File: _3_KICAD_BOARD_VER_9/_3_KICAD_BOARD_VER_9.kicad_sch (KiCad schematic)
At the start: 0 parts

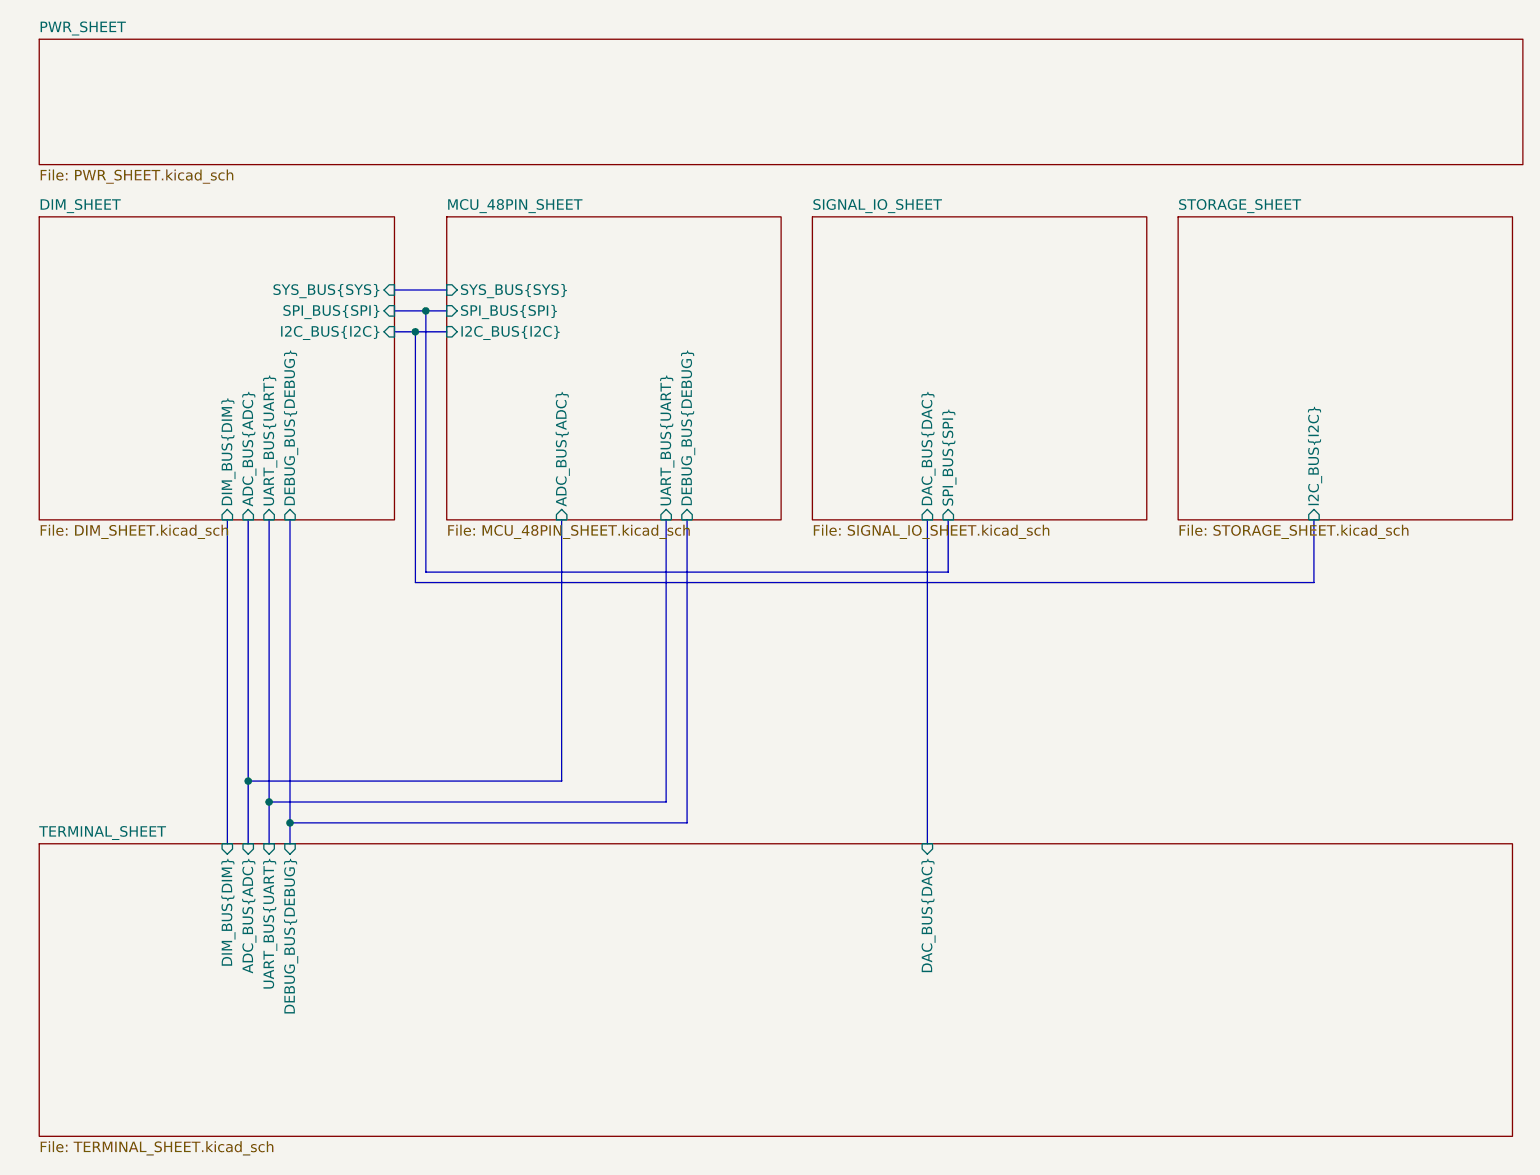
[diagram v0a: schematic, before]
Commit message: feat : vdd, gnd, vin routing done
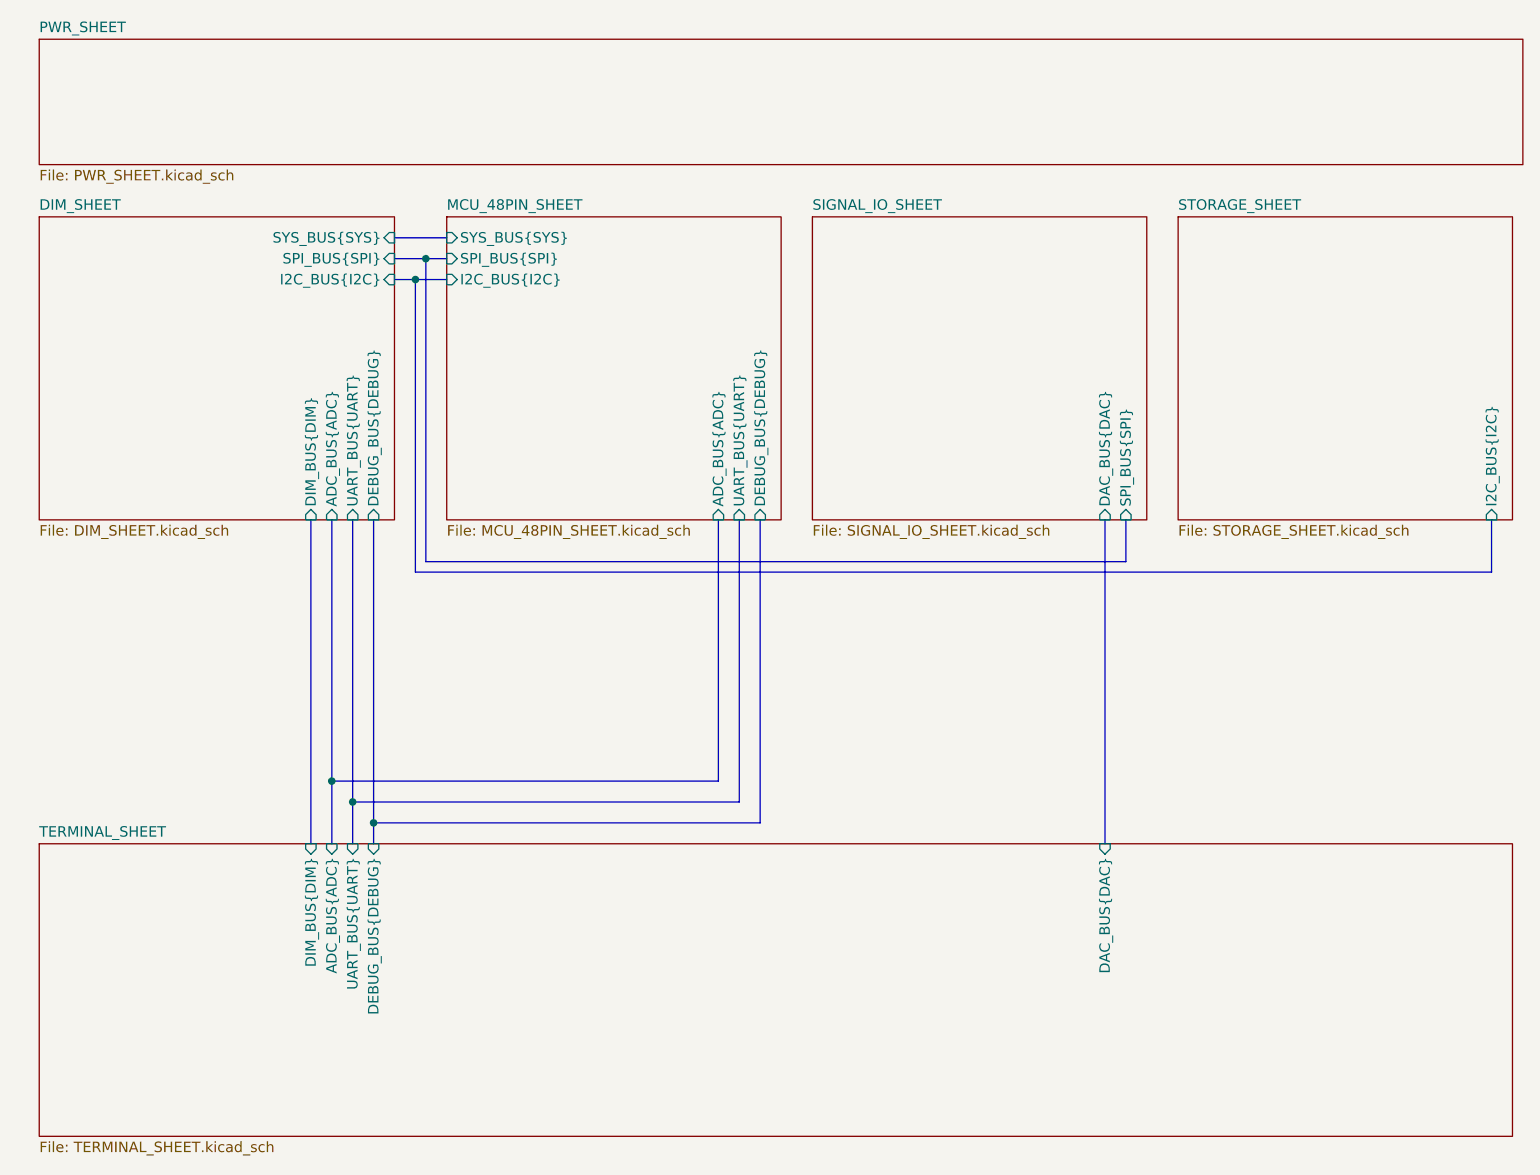
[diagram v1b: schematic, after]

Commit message: feat : dim only project done
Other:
- removed sheet DIM_SHEET
- sheet TERMINAL_SHEET ports: added SYS_BUS{SYS}; removed DIM_BUS{DIM}

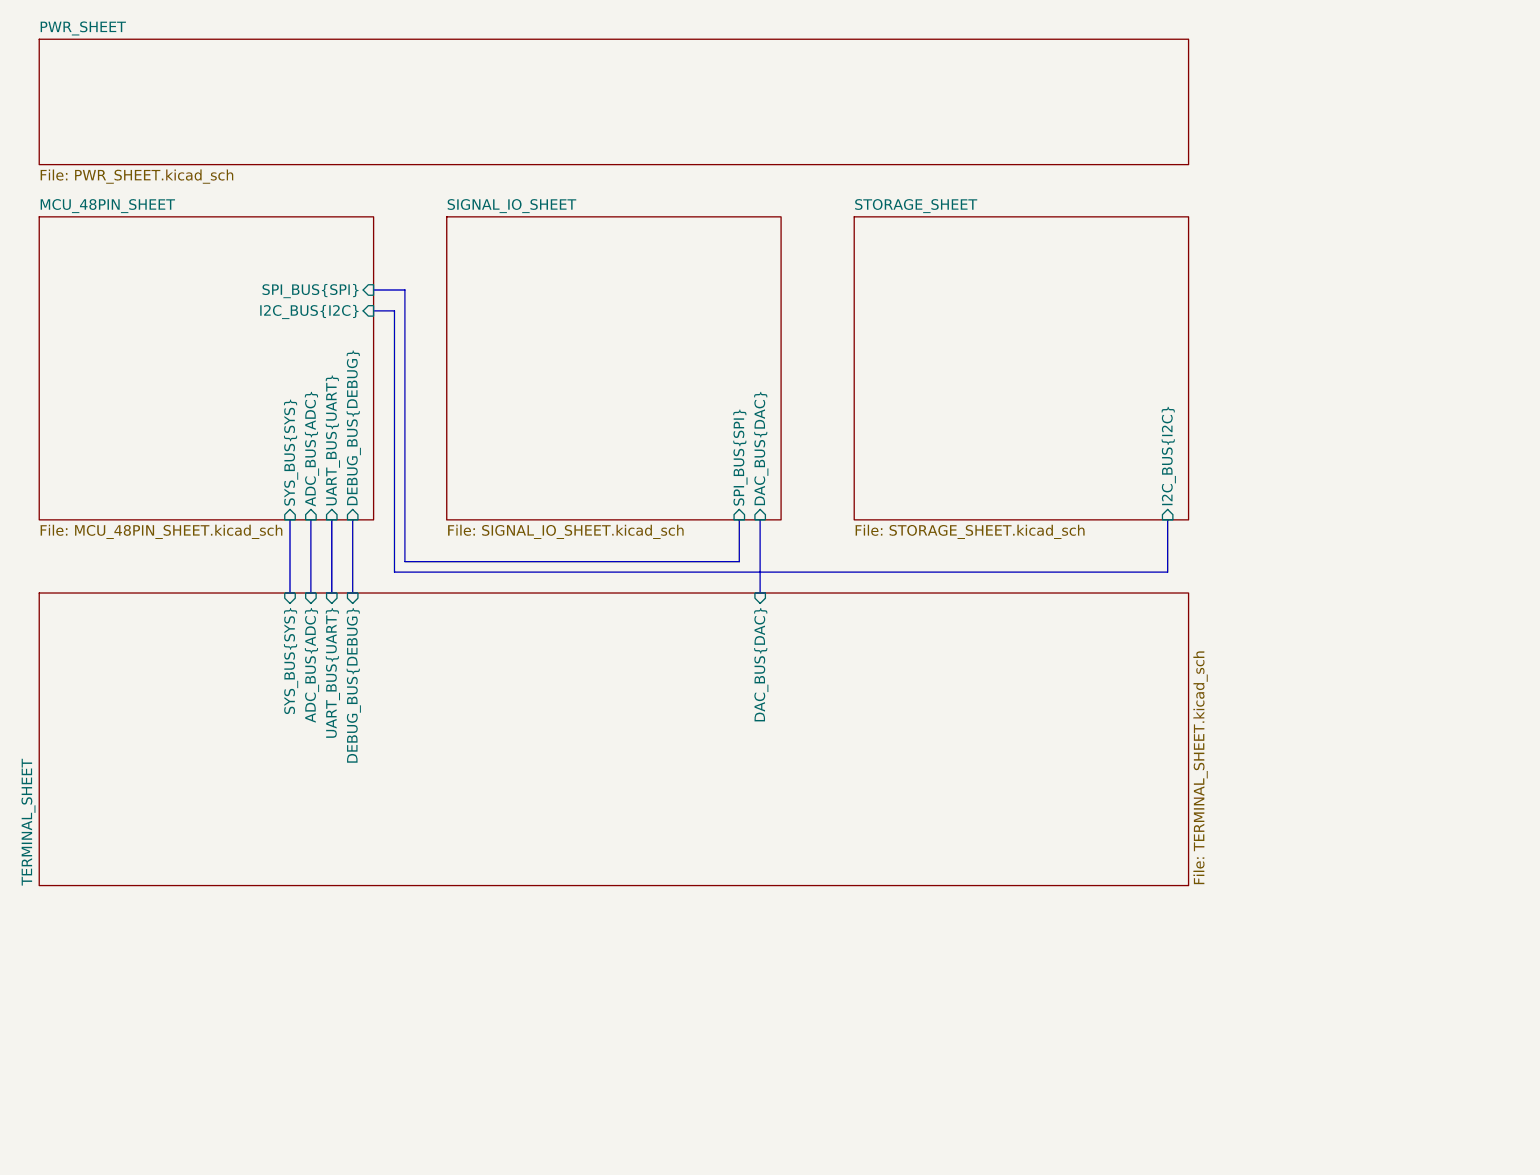
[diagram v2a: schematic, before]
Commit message: feat : 회로도 업데이트
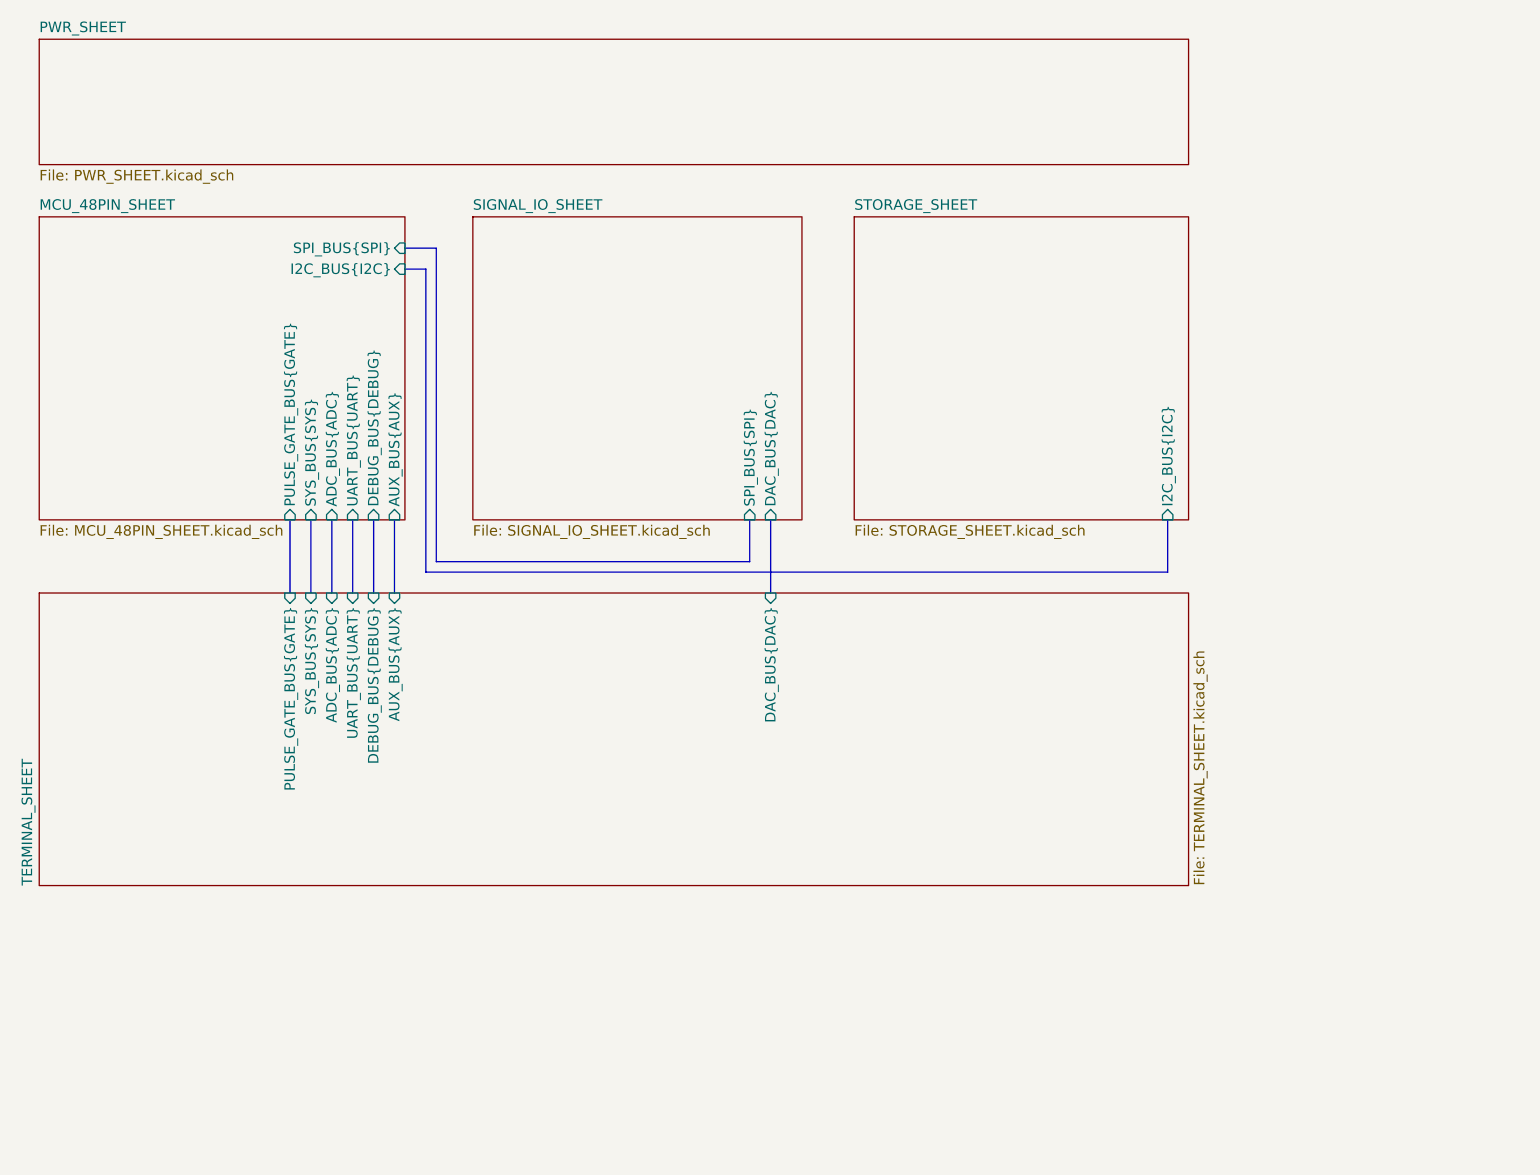
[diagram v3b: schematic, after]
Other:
- sheet MCU_48PIN_SHEET ports: added AUX_BUS{AUX}, PULSE_GATE_BUS{GATE}; removed none
- sheet TERMINAL_SHEET ports: added AUX_BUS{AUX}, PULSE_GATE_BUS{GATE}; removed none
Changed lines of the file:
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@@
+	(bus
+		(pts
+			(xy 77.47 80.01) (xy 77.47 88.9)
+		)
+		(stroke
+			(width 0)
+			(type default)
+		)
+	)
+	(bus
+		(pts
+			(xy 80.01 80.01) (xy 80.01 88.9)
+		)
+		(stroke
+			(width 0)
+			(type default)
+		)
+	)
+	(bus
+		(pts
+			(xy 72.39 80.01) (xy 72.39 88.9)
+		)
+		(stroke
+			(width 0)
+			(type default)
+		)
+	)
+	(bus
+		(pts
+			(xy 82.55 80.01) (xy 82.55 88.9)
+		)
+		(stroke
+			(width 0)
+			(type default)
+		)
+	)
+	(bus
+		(pts
+			(xy 85.09 80.01) (xy 85.09 88.9)
+		)
+		(stroke
+			(width 0)
+			(type default)
+		)
+	)
+	(bus
+		(pts
+			(xy 88.9 86.36) (xy 179.07 86.36)
+		)
+		(stroke
+			(width 0)
+			(type default)
+		)
+	)
+	(bus
+		(pts
+			(xy 88.9 49.53) (xy 86.36 49.53)
+		)
+		(stroke
+			(width 0)
+			(type default)
+		)
+	)
+	(bus
+		(pts
+			(xy 90.17 46.99) (xy 86.36 46.99)
+		)
+		(stroke
+			(width 0)
+			(type default)
+		)
+	)
+	(bus
+		(pts
+			(xy 128.27 80.01) (xy 128.27 85.09)
+		)
+		(stroke
+			(width 0)
+			(type default)
+		)
+	)
+	(bus
+		(pts
+			(xy 179.07 80.01) (xy 179.07 86.36)
+		)
+		(stroke
+			(width 0)
+			(type default)
+		)
+	)
+	(bus
+		(pts
+			(xy 130.81 80.01) (xy 130.81 88.9)
+		)
+		(stroke
+			(width 0)
+			(type default)
+		)
+	)
+	(bus
+		(pts
+			(xy 88.9 49.53) (xy 88.9 86.36)
+		)
+		(stroke
+			(width 0)
+			(type default)
+		)
+	)
+	(bus
+		(pts
+			(xy 90.17 46.99) (xy 90.17 85.09)
+		)
+		(stroke
+			(width 0)
+			(type default)
+		)
+	)
+	(bus
+		(pts
+			(xy 90.17 85.09) (xy 128.27 85.09)
+		)
+		(stroke
+			(width 0)
+			(type default)
+		)
+	)
 	(bus
 		(pts
@@
 		)
 	)
-	(bus
-		(pts
-			(xy 77.47 80.01) (xy 77.47 88.9)
-		)
-		(stroke
-			(width 0)
-			(type default)
-		)
-	)
-	(bus
-		(pts
-			(xy 80.01 80.01) (xy 80.01 88.9)
-		)
-		(stroke
-			(width 0)
-			(type default)
-		)
-	)
-	(bus
-		(pts
-			(xy 85.09 86.36) (xy 179.07 86.36)
-		)
-		(stroke
-			(width 0)
-			(type default)
-		)
-	)
-	(bus
-		(pts
-			(xy 85.09 54.61) (xy 82.55 54.61)
-		)
-		(stroke
-			(width 0)
-			(type default)
-		)
-	)
-	(bus
-		(pts
-			(xy 129.54 80.01) (xy 129.54 88.9)
-		)
-		(stroke
-			(width 0)
-			(type default)
-		)
-	)
-	(bus
-		(pts
-			(xy 86.36 52.07) (xy 82.55 52.07)
-		)
-		(stroke
-			(width 0)
-			(type default)
-		)
-	)
-	(bus
-		(pts
-			(xy 179.07 80.01) (xy 179.07 86.36)
-		)
-		(stroke
-			(width 0)
-			(type default)
-		)
-	)
-	(bus
-		(pts
-			(xy 85.09 54.61) (xy 85.09 86.36)
-		)
-		(stroke
-			(width 0)
-			(type default)
-		)
-	)
-	(bus
-		(pts
-			(xy 86.36 52.07) (xy 86.36 85.09)
-		)
-		(stroke
-			(width 0)
-			(type default)
-		)
-	)
-	(bus
-		(pts
-			(xy 86.36 85.09) (xy 127 85.09)
-		)
-		(stroke
-			(width 0)
-			(type default)
-		)
-	)
-	(bus
-		(pts
-			(xy 127 80.01) (xy 127 85.09)
-		)
-		(stroke
-			(width 0)
-			(type default)
-		)
-	)
-	(bus
-		(pts
-			(xy 72.39 80.01) (xy 72.39 88.9)
-		)
-		(stroke
-			(width 0)
-			(type default)
-		)
-	)
 	(sheet
-		(at 91.44 43.18)
-		(size 40.64 36.83)
+		(at 94.615 43.18)
+		(size 40.005 36.83)
 		(exclude_from_sim no)
 		(in_bom yes)
@@
 		)
 		(property "Sheetname" "SIGNAL_IO_SHEET"
-			(at 91.44 42.4684 0)
+			(at 94.615 42.4684 0)
 			(effects
 				(font
@@
 		)
 		(property "Sheetfile" "SIGNAL_IO_SHEET.kicad_sch"
-			(at 91.44 80.5946 0)
+			(at 94.615 80.5946 0)
 			(effects
 				(font
@@
 		)
 		(pin "DAC_BUS{DAC}" input
-			(at 129.54 80.01 270)
+			(at 130.81 80.01 270)
 			(effects
 				(font
@@
 		)
 		(pin "SPI_BUS{SPI}" input
-			(at 127 80.01 270)
+			(at 128.27 80.01 270)
 			(effects
 				(font
@@
 		)
 		(pin "ADC_BUS{ADC}" input
+			(at 77.47 88.9 90)
+			(effects
+				(font
+					(size 1.27 1.27)
+				)
+				(justify right)
+			)
+		)
+		(pin "DAC_BUS{DAC}" input
+			(at 130.81 88.9 90)
+			(effects
+				(font
+					(size 1.27 1.27)
+				)
+				(justify right)
+			)
+		)
+		(pin "DEBUG_BUS{DEBUG}" input
+			(at 82.55 88.9 90)
+			(effects
+				(font
+					(size 1.27 1.27)
+				)
+				(justify right)
+			)
+		)
+		(pin "UART_BUS{UART}" input
+			(at 80.01 88.9 90)
+			(effects
+				(font
+					(size 1.27 1.27)
+				)
+				(justify right)
+			)
+		)
+		(pin "SYS_BUS{SYS}" input
 			(at 74.93 88.9 90)
 			(effects
@@
 			)
 		)
-		(pin "DAC_BUS{DAC}" input
-			(at 129.54 88.9 90)
-			(effects
-				(font
-					(size 1.27 1.27)
-				)
-				(justify right)
-			)
-		)
-		(pin "DEBUG_BUS{DEBUG}" input
-			(at 80.01 88.9 90)
-			(effects
-				(font
-					(size 1.27 1.27)
-				)
-				(justify right)
-			)
-		)
-		(pin "UART_BUS{UART}" input
-			(at 77.47 88.9 90)
-			(effects
-				(font
-					(size 1.27 1.27)
-				)
-				(justify right)
-			)
-		)
-		(pin "SYS_BUS{SYS}" input
+		(pin "PULSE_GATE_BUS{GATE}" input
 			(at 72.39 88.9 90)
+			(effects
+				(font
+					(size 1.27 1.27)
+				)
+				(justify right)
+			)
+		)
+		(pin "AUX_BUS{AUX}" input
+			(at 85.09 88.9 90)
 			(effects
 				(font
@@
 	(sheet
 		(at 41.91 43.18)
-		(size 40.64 36.83)
+		(size 44.45 36.83)
 		(exclude_from_sim no)
 		(in_bom yes)
@@
 		)
 		(pin "ADC_BUS{ADC}" input
+			(at 77.47 80.01 270)
+			(effects
+				(font
+					(size 1.27 1.27)
+				)
+				(justify left)
+			)
+		)
+		(pin "DEBUG_BUS{DEBUG}" input
+			(at 82.55 80.01 270)
+			(effects
+				(font
+					(size 1.27 1.27)
+				)
+				(justify left)
+			)
+		)
+		(pin "I2C_BUS{I2C}" input
+			(at 86.36 49.53 0)
+			(effects
+				(font
+					(size 1.27 1.27)
+				)
+				(justify right)
+			)
+		)
+		(pin "SPI_BUS{SPI}" input
+			(at 86.36 46.99 0)
+			(effects
+				(font
+					(size 1.27 1.27)
+				)
+				(justify right)
+			)
+		)
+		(pin "UART_BUS{UART}" input
+			(at 80.01 80.01 270)
+			(effects
+				(font
+					(size 1.27 1.27)
+				)
+				(justify left)
+			)
+		)
+		(pin "SYS_BUS{SYS}" input
 			(at 74.93 80.01 270)
 			(effects
@@
 			)
 		)
-		(pin "DEBUG_BUS{DEBUG}" input
-			(at 80.01 80.01 270)
-			(effects
-				(font
-					(size 1.27 1.27)
-				)
-				(justify left)
-			)
-		)
-		(pin "I2C_BUS{I2C}" input
-			(at 82.55 54.61 0)
-			(effects
-				(font
-					(size 1.27 1.27)
-				)
-				(justify right)
-			)
-		)
-		(pin "SPI_BUS{SPI}" input
-			(at 82.55 52.07 0)
-			(effects
-				(font
-					(size 1.27 1.27)
-				)
-				(justify right)
-			)
-		)
-		(pin "UART_BUS{UART}" input
-			(at 77.47 80.01 270)
-			(effects
-				(font
-					(size 1.27 1.27)
-				)
-				(justify left)
-			)
-		)
-		(pin "SYS_BUS{SYS}" input
+		(pin "PULSE_GATE_BUS{GATE}" input
 			(at 72.39 80.01 270)
 			(effects
 				(font
+					(size 1.27 1.27)
+				)
+				(justify left)
+			)
+		)
+		(pin "AUX_BUS{AUX}" input
+			(at 85.09 80.01 270)
+			(effects
+				(font
